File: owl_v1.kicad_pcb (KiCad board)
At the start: 2 copper layers, 11 parts, among them U1 STM32F103C8T6, U2 XC6206P302

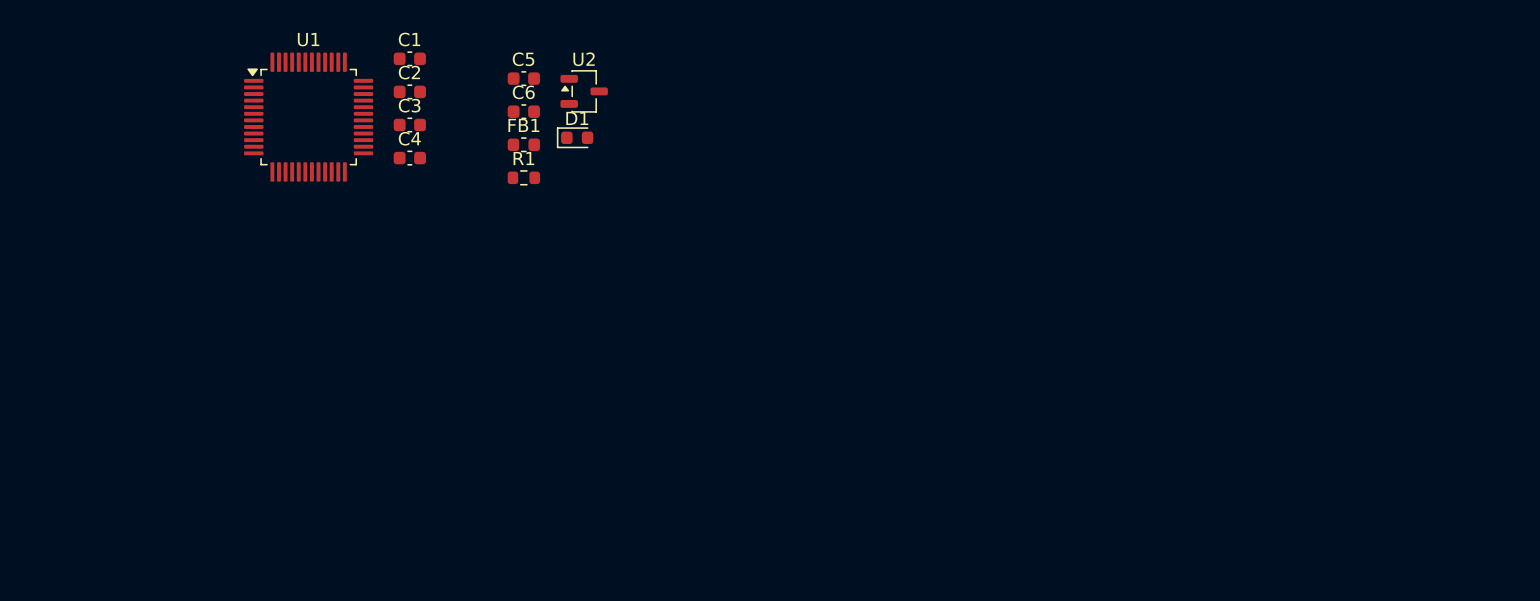
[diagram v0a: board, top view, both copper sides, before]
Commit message: [fix] Add 5.1kR to CC1 and CC2 USB
USB-C specification requires CC1 and CC2 to be connected to ground via a
resistor for USB-C to USB-C power to work.
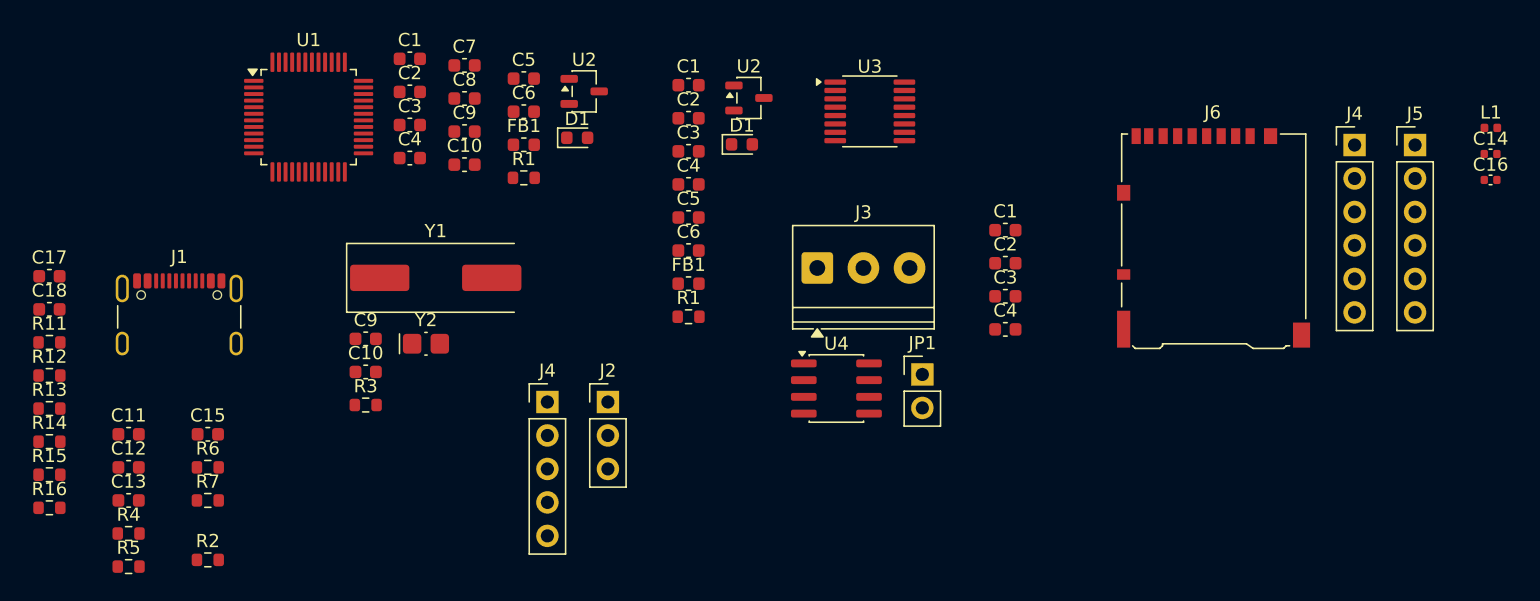
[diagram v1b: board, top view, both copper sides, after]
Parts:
- added C1: 10u, Capacitor_SMD:C_0603_1608Metric, F.Cu at (158.5, 91.3)
- added C1: 10u, Capacitor_SMD:C_0603_1608Metric, F.Cu at (182.5, 102.3)
- added C10: 30p, Capacitor_SMD:C_0603_1608Metric, F.Cu at (141.5, 97.3)
- added C10: 4p, Capacitor_SMD:C_0603_1608Metric, F.Cu at (134.0, 113.0)
- added C11: 47p, Capacitor_SMD:C_0603_1608Metric, F.Cu at (116.0, 117.7)
- added C12: 47p, Capacitor_SMD:C_0603_1608Metric, F.Cu at (116.0, 120.3)
- added C13: 100n, Capacitor_SMD:C_0603_1608Metric, F.Cu at (116.0, 122.8)
- added C14: 1u, Capacitor_SMD:C_0402_1005Metric, F.Cu at (219.4, 96.5)
- added C15: 100nF, Capacitor_SMD:C_0603_1608Metric, F.Cu at (122.0, 117.7)
- added C16: 100n, Capacitor_SMD:C_0402_1005Metric, F.Cu at (219.4, 98.4)
- added C17: 10uF, Capacitor_SMD:C_0603_1608Metric, F.Cu at (110.0, 105.8)
- added C18: 100nF, Capacitor_SMD:C_0603_1608Metric, F.Cu at (110.0, 108.3)
- added C2: 100n, Capacitor_SMD:C_0603_1608Metric, F.Cu at (158.5, 93.8)
- added C2: 100n, Capacitor_SMD:C_0603_1608Metric, F.Cu at (182.5, 104.8)
- added C3: 100n, Capacitor_SMD:C_0603_1608Metric, F.Cu at (158.5, 96.3)
- added C3: 100n, Capacitor_SMD:C_0603_1608Metric, F.Cu at (182.5, 107.3)
- added C4: 100n, Capacitor_SMD:C_0603_1608Metric, F.Cu at (182.5, 109.8)
- added C4: 100n, Capacitor_SMD:C_0603_1608Metric, F.Cu at (158.5, 98.8)
- added C5: 1u, Capacitor_SMD:C_0603_1608Metric, F.Cu at (158.5, 101.3)
- added C6: 1u, Capacitor_SMD:C_0603_1608Metric, F.Cu at (158.5, 103.8)
- added C7: 25p, Capacitor_SMD:C_0603_1608Metric, F.Cu at (141.5, 89.8)
- added C8: 25p, Capacitor_SMD:C_0603_1608Metric, F.Cu at (141.5, 92.3)
- added C9: 4p, Capacitor_SMD:C_0603_1608Metric, F.Cu at (134.0, 110.5)
- added C9: 30p, Capacitor_SMD:C_0603_1608Metric, F.Cu at (141.5, 94.8)
- added D1: GREEN, LED_SMD:LED_0603_1608Metric, F.Cu at (162.6, 95.7)
- added FB1: 100R, Inductor_SMD:L_0603_1608Metric, F.Cu at (158.5, 106.3)
- added J1: USB_C_Receptacle_USB2.0_14P, Connector_USB:USB_C_Receptacle_GCT_USB4105-xx-A_16P_TopMnt_Horizontal, F.Cu at (119.9, 109.8)
- added J2: SWD, Connector_PinHeader_2.54mm:PinHeader_1x03_P2.54mm_Vertical, F.Cu at (152.4, 115.3)
- added J3: Screw_Terminal_01x03, TerminalBlock_Phoenix:TerminalBlock_Phoenix_PT-1,5-3-3.5-H_1x03_P3.50mm_Horizontal, F.Cu at (168.3, 105.1)
- added J4: SPI1_IMU, Connector_PinHeader_2.54mm:PinHeader_1x06_P2.54mm_Vertical, F.Cu at (209.0, 95.8)
- added J4: SPI1 IMU, Connector_PinHeader_2.54mm:PinHeader_1x05_P2.54mm_Vertical, F.Cu at (147.8, 115.3)
- added J5: SPI1_IMU, Connector_PinHeader_2.54mm:PinHeader_1x06_P2.54mm_Vertical, F.Cu at (213.6, 95.8)
- added J6: Micro_SD_Card_Det_Hirose_DM3AT, Connector_Card:microSD_HC_Hirose_DM3AT-SF-PEJM5, F.Cu at (198.3, 102.8)
- added JP1: Jumper_2_Open, Connector_PinHeader_2.54mm:PinHeader_1x02_P2.54mm_Vertical, F.Cu at (176.2, 113.2)
- added L1: 27n, Inductor_SMD:L_0402_1005Metric, F.Cu at (219.4, 94.5)
- added R1: 1k5, Resistor_SMD:R_0603_1608Metric, F.Cu at (158.5, 108.8)
- added R11: 10kR, Resistor_SMD:R_0603_1608Metric, F.Cu at (110.0, 110.8)
- added R12: 47kR, Resistor_SMD:R_0603_1608Metric, F.Cu at (110.0, 113.3)
- added R13: 47kR, Resistor_SMD:R_0603_1608Metric, F.Cu at (110.0, 115.8)
- added R14: 47kR, Resistor_SMD:R_0603_1608Metric, F.Cu at (110.0, 118.3)
- added R15: 47kR, Resistor_SMD:R_0603_1608Metric, F.Cu at (110.0, 120.8)
- added R16: 47kR, Resistor_SMD:R_0603_1608Metric, F.Cu at (110.0, 123.3)
- added R2: 100k, Resistor_SMD:R_0603_1608Metric, F.Cu at (122.0, 127.3)
- added R3: 0R, Resistor_SMD:R_0603_1608Metric, F.Cu at (134.0, 115.5)
- added R4: 27R, Resistor_SMD:R_0603_1608Metric, F.Cu at (116.0, 125.3)
- added R5: 27R, Resistor_SMD:R_0603_1608Metric, F.Cu at (116.0, 127.8)
- added R6: 0R, Resistor_SMD:R_0603_1608Metric, F.Cu at (122.0, 120.3)
- added R7: 120R, Resistor_SMD:R_0603_1608Metric, F.Cu at (122.0, 122.8)
- added U2: XC6206P302, Package_TO_SOT_SMD:SOT-23-3, F.Cu at (163.1, 92.2)
- added U3: FT230XS, Package_SO:SSOP-16_3.9x4.9mm_P0.635mm, F.Cu at (172.3, 93.2)
- added U4: SN65HVD230, Package_SO:SOIC-8_3.9x4.9mm_P1.27mm, F.Cu at (169.7, 114.3)
- added Y1: 8MHz, Crystal:Crystal_SMD_HC49-SD, F.Cu at (139.3, 105.9)
- added Y2: 32k768, Crystal:Crystal_SMD_MicroCrystal_CC8V-T1A-2Pin_2.0x1.2mm_HandSoldering, F.Cu at (138.6, 110.9)
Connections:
- U1 pad 14: unconnected-(U1-PA4-Pad14) -> SPI1_CS
- U1 pad 15: unconnected-(U1-PA5-Pad15) -> SPI1_SCK
- U1 pad 16: unconnected-(U1-PA6-Pad16) -> SPI1_MISO
- U1 pad 17: unconnected-(U1-PA7-Pad17) -> SPI1_MOSI
- U1 pad 23: Net-(U1-VSS-Pad23) -> +3.3V
- U1 pad 25: unconnected-(U1-PB12-Pad25) -> SD_CS
- U1 pad 26: unconnected-(U1-PB13-Pad26) -> SD_SCK
- U1 pad 27: unconnected-(U1-PB14-Pad27) -> SD_MISO
- U1 pad 28: unconnected-(U1-PB15-Pad28) -> SD_MOSI
- U1 pad 3: unconnected-(U1-PC14-Pad3) -> LSE_OSC_IN
- U1 pad 30: unconnected-(U1-PA9-Pad30) -> /USB to UART Bridge/FT230_RXD
- U1 pad 31: unconnected-(U1-PA10-Pad31) -> /USB to UART Bridge/FT230_TXD
- U1 pad 34: unconnected-(U1-PA13-Pad34) -> SWDIO
- U1 pad 35: Net-(U1-VSS-Pad23) -> +3.3V
- U1 pad 37: unconnected-(U1-PA14-Pad37) -> SWCLK
- U1 pad 39: unconnected-(U1-PB3-Pad39) -> TRACE_SWO
- U1 pad 4: unconnected-(U1-PC15-Pad4) -> LSE_OSC_OUT
- U1 pad 44: unconnected-(U1-BOOT0-Pad44) -> Net-(U1-BOOT0)
- U1 pad 45: unconnected-(U1-PB8-Pad45) -> CAN_RX
- U1 pad 46: unconnected-(U1-PB9-Pad46) -> CAN_TX
- U1 pad 47: Net-(U1-VSS-Pad23) -> +3.3V
- U1 pad 5: unconnected-(U1-PD0-Pad5) -> HSE_OSC_IN
- U1 pad 6: unconnected-(U1-PD1-Pad6) -> HSE_OSC_OUT
- U1 pad 8: unconnected-(U1-VSSA-Pad8) -> +3.3V
- U1 pad 9: unconnected-(U1-VDDA-Pad9) -> +3.3VA

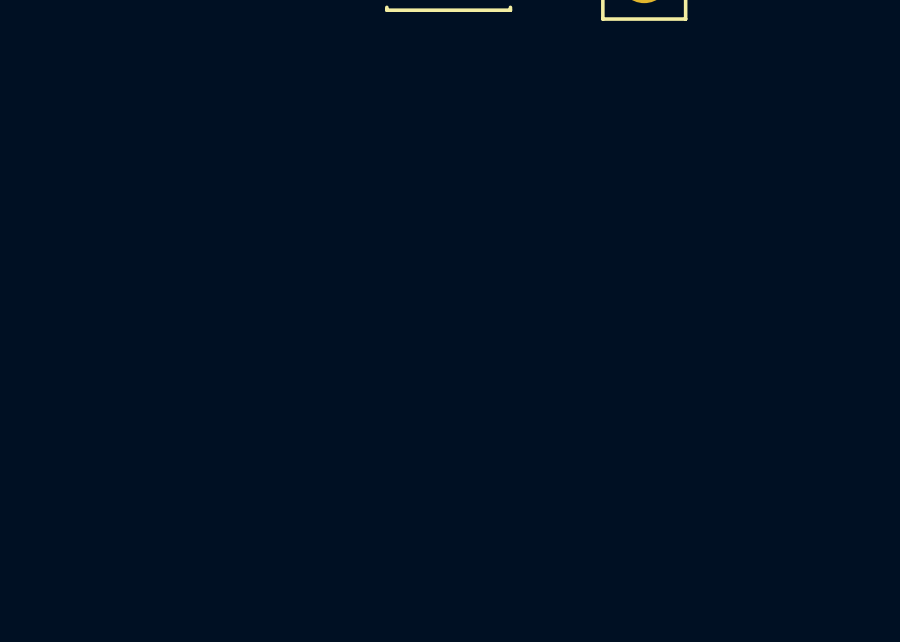
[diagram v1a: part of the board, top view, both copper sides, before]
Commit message: [feat] Add OLED I2C breakout for display, Add general purpose GPIOs
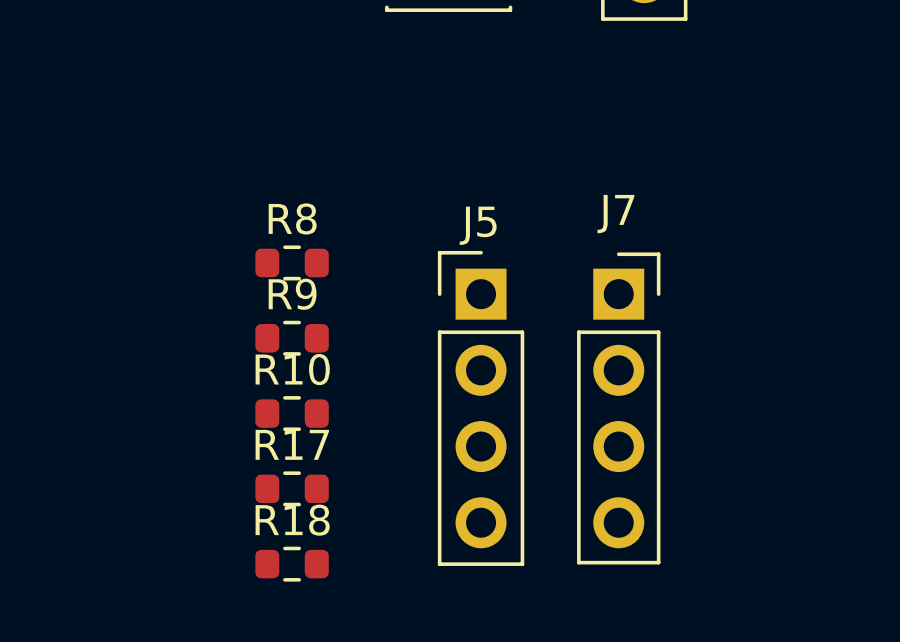
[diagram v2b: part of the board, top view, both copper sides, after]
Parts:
- added J5: I2C, Connector_PinHeader_2.54mm:PinHeader_1x04_P2.54mm_Vertical, F.Cu at (170.8, 126.3)
- added J7: I2C OLED, Connector_PinSocket_2.54mm:PinSocket_1x04_P2.54mm_Vertical, F.Cu at (175.4, 126.3)
- added R10: 1kR, Resistor_SMD:R_0603_1608Metric, F.Cu at (164.5, 130.3)
- added R17: 1kR, Resistor_SMD:R_0603_1608Metric, F.Cu at (164.5, 132.8)
- added R18: 1kR, Resistor_SMD:R_0603_1608Metric, F.Cu at (164.5, 135.3)
- added R8: 5k1R, Resistor_SMD:R_0603_1608Metric, F.Cu at (164.5, 125.3)
- added R9: 5k1R, Resistor_SMD:R_0603_1608Metric, F.Cu at (164.5, 127.8)
- J1: value USB_C_Receptacle_USB2.0_14P -> USB_C_Receptacle_USB2.0_16P
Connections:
- C1 pad 2: +3.3V -> GND
- C10 pad 2: +3.3V -> GND
- C11 pad 2: +3.3V -> GND
- C12 pad 2: +3.3V -> GND
- C13 pad 1: +3.3V -> GND
- C14 pad 2: +3.3V -> GND
- C15 pad 2: +3.3V -> GND
- C16 pad 2: +3.3V -> GND
- C17 pad 2: +3.3V -> GND
- C18 pad 2: +3.3V -> GND
- C2 pad 2: +3.3V -> GND
- C3 pad 2: +3.3V -> GND
- C4 pad 2: +3.3V -> GND
- C5 pad 2: +3.3V -> GND
- C6 pad 2: +3.3V -> GND
- C7 pad 2: +3.3V -> GND
- C8 pad 2: +3.3V -> GND
- C9 pad 2: +3.3V -> GND
- J1 pad A1: +3.3V -> GND
- J1 pad A12: +3.3V -> GND
- J1 pad A5: unconnected-(J1-CC1-PadA5) -> Net-(J1-CC1)
- J1 pad A8: (no net) -> unconnected-(J1-SBU1-PadA8)
- J1 pad B1: +3.3V -> GND
- J1 pad B12: +3.3V -> GND
- J1 pad B5: unconnected-(J1-CC2-PadB5) -> Net-(J1-CC2)
- J1 pad B8: (no net) -> unconnected-(J1-SBU2-PadB8)
- J1 pad SH: unconnected-(J1-SHIELD-PadSH) -> GND
- J3 pad 3: +3.3V -> GND
- J4 pad 6: +3.3V -> GND
- J6 pad 6: +3.3V -> GND
- J6 pad 9: +3.3V -> GND
- R6 pad 1: +3.3V -> GND
- U1 pad 10: unconnected-(U1-PA0-Pad10) -> GPIO_0
- U1 pad 11: unconnected-(U1-PA1-Pad11) -> GPIO_1
- U1 pad 12: unconnected-(U1-PA2-Pad12) -> GPIO_2
- U1 pad 13: unconnected-(U1-PA3-Pad13) -> GPIO_3
- U1 pad 21: unconnected-(U1-PB10-Pad21) -> OLED_SCLK
- U1 pad 22: unconnected-(U1-PB11-Pad22) -> OLED_SDA
- U1 pad 23: +3.3V -> GND
- U1 pad 35: +3.3V -> GND
- U1 pad 42: unconnected-(U1-PB6-Pad42) -> I2C_SCLK
- U1 pad 43: unconnected-(U1-PB7-Pad43) -> I2C_SDA
- U1 pad 47: +3.3V -> GND
- U1 pad 8: +3.3V -> GND
- U2 pad 1: +3.3V -> GND
- U3 pad 13: +3.3V -> GND
- U3 pad 5: +3.3V -> GND
- U4 pad 2: +3.3V -> GND

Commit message: [refactor] Remove GPIO12 and GPIO13 for LED green and blue
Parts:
- added J8: External GPIOs, Connector_PinHeader_2.54mm:PinHeader_1x13_P2.54mm_Vertical, F.Cu at (185.3, 121.8)
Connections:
- net /CAN Transceiver/CAN_H renamed /owl_v1/CAN Transceiver/CAN_H
- net /CAN Transceiver/CAN_L renamed /owl_v1/CAN Transceiver/CAN_L
- net /USB Power Regulator/LED_BLUE renamed /owl_v1/Power Regulation/LED_BLUE
- net /USB Power Regulator/LED_GREEN renamed /owl_v1/Power Regulation/LED_GREEN
- net /USB Power Regulator/USB_OUT_D+ renamed /owl_v1/Power Regulation/USB_OUT_D+
- net /USB Power Regulator/USB_OUT_D- renamed /owl_v1/Power Regulation/USB_OUT_D-
- net /USB to UART Bridge/FT230_RXD renamed /owl_v1/USB to UART Bridge/FT230_RXD
- net /USB to UART Bridge/FT230_TXD renamed /owl_v1/USB to UART Bridge/FT230_TXD
- U1 pad 18: unconnected-(U1-PB0-Pad18) -> GPIO_9
- U1 pad 19: unconnected-(U1-PB1-Pad19) -> GPIO_10
- U1 pad 2: unconnected-(U1-PC13-Pad2) -> GPIO_8
- U1 pad 20: unconnected-(U1-PB2-Pad20) -> GPIO_11
- U1 pad 29: unconnected-(U1-PA8-Pad29) -> GPIO_4
- U1 pad 32: unconnected-(U1-PA11-Pad32) -> GPIO_5
- U1 pad 33: unconnected-(U1-PA12-Pad33) -> GPIO_6
- U1 pad 38: unconnected-(U1-PA15-Pad38) -> GPIO_7
- U1 pad 40: unconnected-(U1-PB4-Pad40) -> GPIO_12
- U1 pad 41: unconnected-(U1-PB5-Pad41) -> GPIO_13

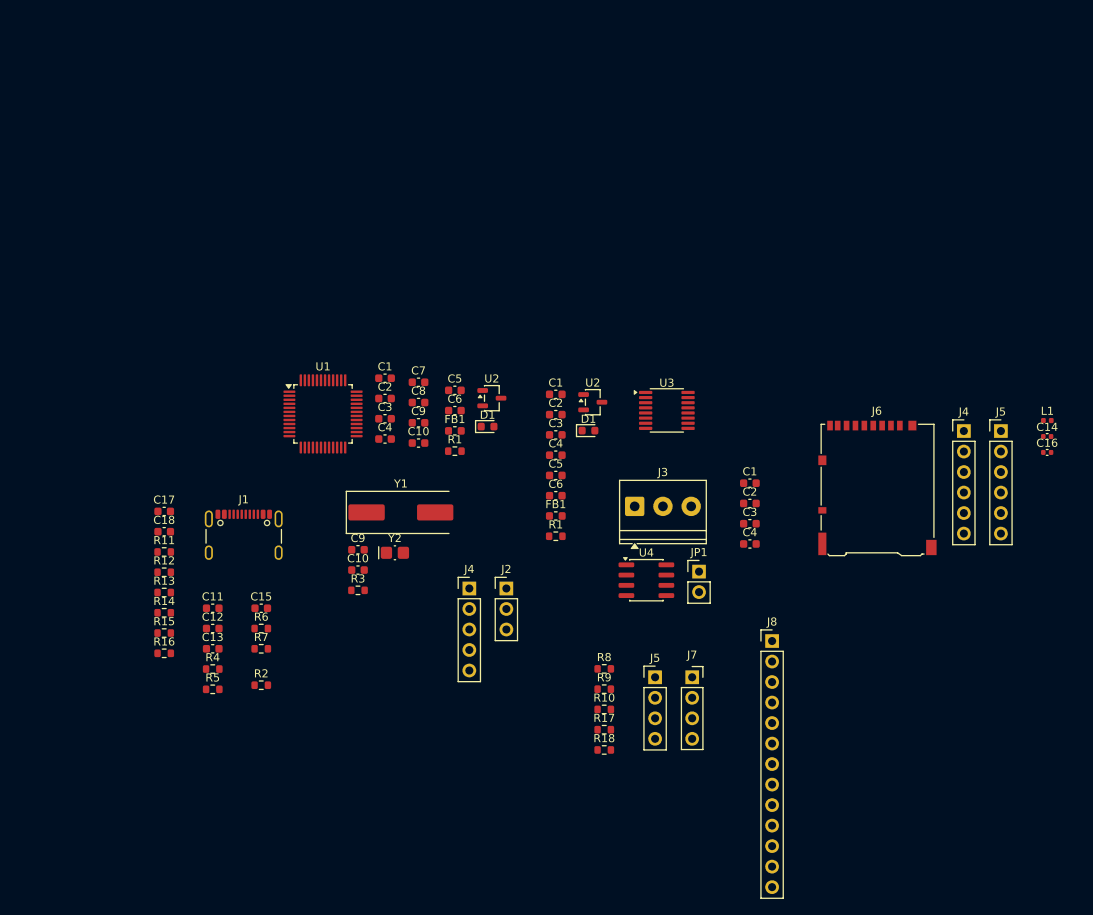
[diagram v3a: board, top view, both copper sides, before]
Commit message: [feat] Integrate external battery
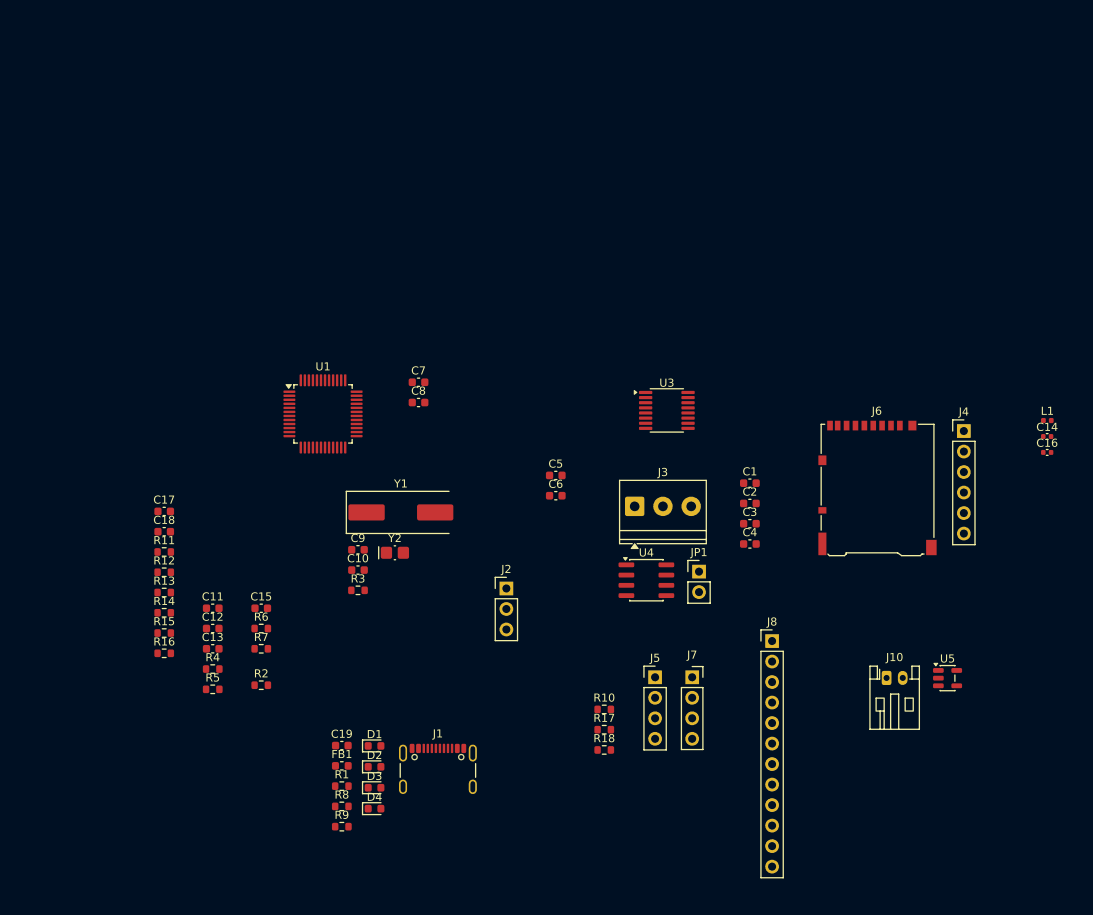
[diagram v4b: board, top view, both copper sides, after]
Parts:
- removed the C1 at (158.5, 91.3)
- removed the C1 at (137.4, 89.3)
- removed the C10 at (141.5, 97.3)
- removed the C2 at (158.5, 93.8)
- removed the C2 at (137.4, 91.8)
- removed the C3 at (158.5, 96.3)
- removed the C3 at (137.4, 94.3)
- removed the C4 at (158.5, 98.8)
- removed the C4 at (137.4, 96.8)
- removed the C5 at (146.0, 90.8)
- removed the C6 at (146.0, 93.3)
- removed the C9 at (141.5, 94.8)
- removed the D1 at (162.6, 95.7)
- removed the D1 at (150.1, 95.2)
- removed the FB1 at (158.5, 106.3)
- removed the FB1 at (146.0, 95.8)
- removed the J4 at (147.8, 115.3)
- removed the J5 at (213.6, 95.8)
- removed the R1 at (146.0, 98.3)
- removed the R1 at (158.5, 108.8)
- removed U2 (x2): XC6206P302, Package_TO_SOT_SMD:SOT-23-3
- added C19: 1uF, Capacitor_SMD:C_0603_1608Metric, F.Cu at (132.0, 134.8)
- added D1: RED, LED_SMD:LED_0603_1608Metric, F.Cu at (136.1, 134.8)
- added D2: GREEN, LED_SMD:LED_0603_1608Metric, F.Cu at (136.1, 137.4)
- added D3: BLUE, LED_SMD:LED_0603_1608Metric, F.Cu at (136.1, 140.0)
- added D4: D_Schottky, Diode_SMD:D_0603_1608Metric, F.Cu at (136.1, 142.6)
- added FB1: 100R, Inductor_SMD:L_0603_1608Metric, F.Cu at (132.0, 137.3)
- added J10: JST-PH Battery, Connector_JST:JST_PH_S2B-PH-K_1x02_P2.00mm_Horizontal, F.Cu at (199.5, 126.4)
- added R1: 10kR, Resistor_SMD:R_0603_1608Metric, F.Cu at (132.0, 139.8)
- added U5: TLV73333PDBV, Package_TO_SOT_SMD:SOT-23-5, F.Cu at (207.0, 126.4)
- C1: value 10u -> 10uF
- C10, C9: value 4p -> 4pF
- C11, C12: value 47p -> 47pF
- C13, C16, C2, C3, C4: value 100n -> 100nF
- C14, C5, C6: value 1u -> 1uF
- C7, C8: value 25p -> 25pF
- J8: footprint Connector_PinHeader_2.54mm:PinHeader_1x13_P2.54mm_Vertical -> Connector_PinHeader_2.54mm:PinHeader_1x12_P2.54mm_Vertical
- L1: value 27n -> 27nH
- R2: value 100k -> 100kR
- moved J1 37.7 mm to (143.9, 138.8)
- moved R8 36.7 mm to (132.0, 142.3)
- moved R9 36.7 mm to (132.0, 144.8)
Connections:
- C5 pad 1: Net-(U2-VI) -> VBUS
- R17 pad 2: /owl_v1/Power Regulation/LED_GREEN -> LED_GREEN
- R18 pad 2: /owl_v1/Power Regulation/LED_BLUE -> LED_BLUE
- U1 pad 40: GPIO_12 -> LED_BLUE
- U1 pad 41: GPIO_13 -> LED_GREEN
